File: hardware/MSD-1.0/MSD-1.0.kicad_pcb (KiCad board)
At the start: 2 copper layers, 98.4 x 31.7 mm, 19 parts, among them J1 Conn_01x05, J2 Conn_01x03, Q1 IRF840N, U1 NE555P, U2 PC817, U3 PC817

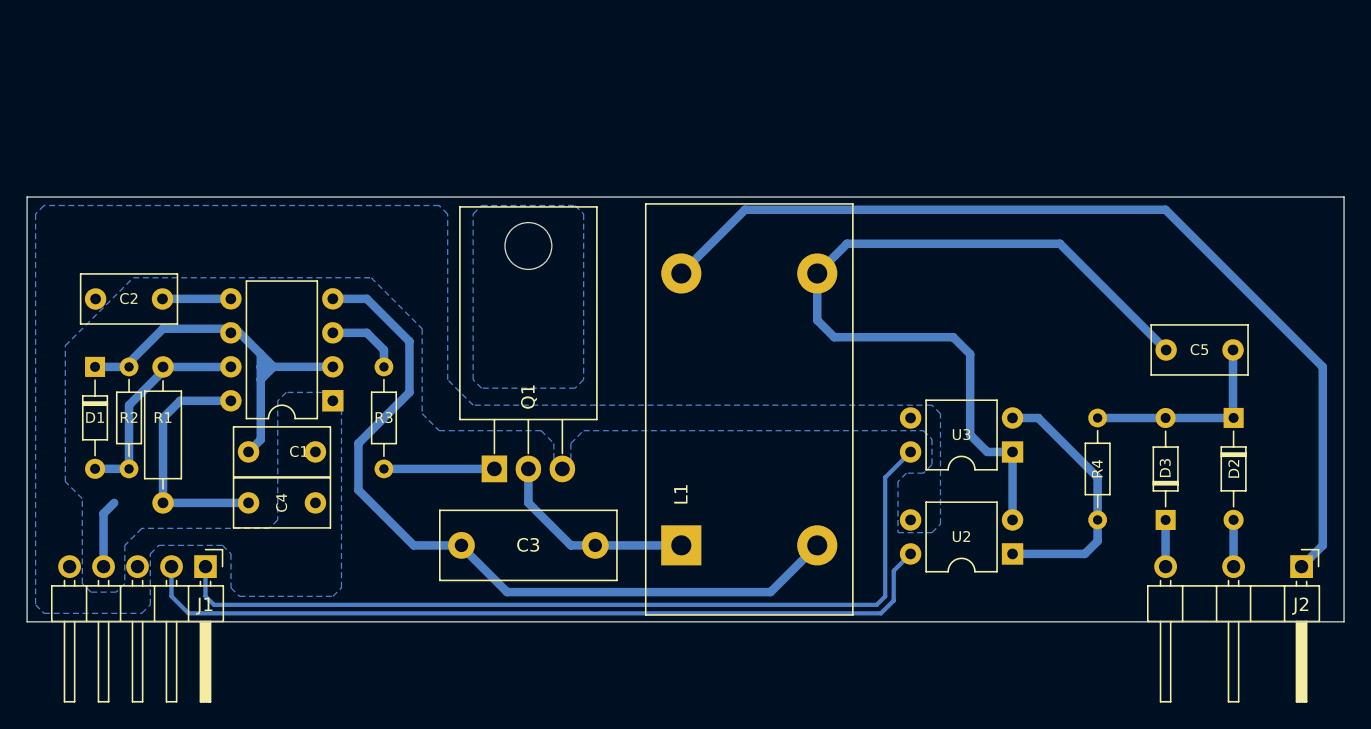
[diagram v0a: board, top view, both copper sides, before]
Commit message: deleted:    hardware/MSD-1.0/#auto_saved_files# 	new file:   hardware/MSD-1.0/MSD-1.0 BoM.csv 	new file:   hardware/MSD-1.0/MSD-1.0-B_Cu.gbr 	new file:   hardware/MSD-1.0/MSD-1.0-B_Mask.gbr 	new file:   hardware/MSD-1.0/MSD-1.0-B_Paste.gbr 	new file:   hardware/MSD-1.0/MSD-1.0-B_Silkscreen.gbr 	new file:   hardware/MSD-1.0/MSD-1.0-Edge_Cuts.gbr 	new file:   hardware/MSD-1.0/MSD-1.0-F_Cu.gbr 	new file:   hardware/MSD-1.0/MSD-1.0-F_Mask.gbr 	new file:   hardware/MSD-1.0/MSD-1.0-F_Paste.gbr 	new file:   hardware/MSD-1.0/MSD-1.0-F_Silkscreen.gbr 	new file:   hardware/MSD-1.0/MSD-1.0-NPTH.drl 	new file:   hardware/MSD-1.0/MSD-1.0-PTH.drl 	deleted:    hardware/MSD-1.0/MSD-1.0-backups/MSD-1.0-2025-02-24_160102.zip 	deleted:    hardware/MSD-1.0/MSD-1.0-backups/MSD-1.0-2025-02-24_160721.zip 	deleted:    hardware/MSD-1.0/MSD-1.0-backups/MSD-1.0-2025-02-24_161316.zip 	deleted:    hardware/MSD-1.0/MSD-1.0-backups/MSD-1.0-2025-02-24_162407.zip 	deleted:    hardware/MSD-1.0/MSD-1.0-backups/MSD-1.0-2025-02-24_163137.zip 	deleted:    hardware/MSD-1.0/MSD-1.0-backups/MSD-1.0-2025-02-25_161045.zip 	deleted:    hardware/MSD-1.0/MSD-1.0-backups/MSD-1.0-2025-02-26_093224.zip 	deleted:    hardware/MSD-1.0/MSD-1.0-backups/MSD-1.0-2025-02-26_094218.zip 	new file:   hardware/MSD-1.0/MSD-1.0-backups/MSD-1.0-2025-02-26_163854.zip 	new file:   hardware/MSD-1.0/MSD-1.0-backups/MSD-1.0-2025-02-27_112851.zip 	new file:   hardware/MSD-1.0/MSD-1.0-backups/MSD-1.0-2025-02-27_114053.zip 	new file:   hardware/MSD-1.0/MSD-1.0-backups/MSD-1.0-2025-02-27_185834.zip 	new file:   hardware/MSD-1.0/MSD-1.0-backups/MSD-1.0-2025-02-27_190654.zip 	new file:   hardware/MSD-1.0/MSD-1.0-backups/MSD-1.0-2025-02-27_191228.zip 	new file:   hardware/MSD-1.0/MSD-1.0-backups/MSD-1.0-2025-02-28_140545.zip 	new file:   hardware/MSD-1.0/MSD-1.0-backups/MSD-1.0-2025-02-28_141533.zip 	new file:   hardware/MSD-1.0/MSD-1.0-backups/MSD-1.0-2025-02-28_142536.zip 	new file:   hardware/MSD-1.0/MSD-1.0-backups/MSD-1.0-2025-02-28_14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
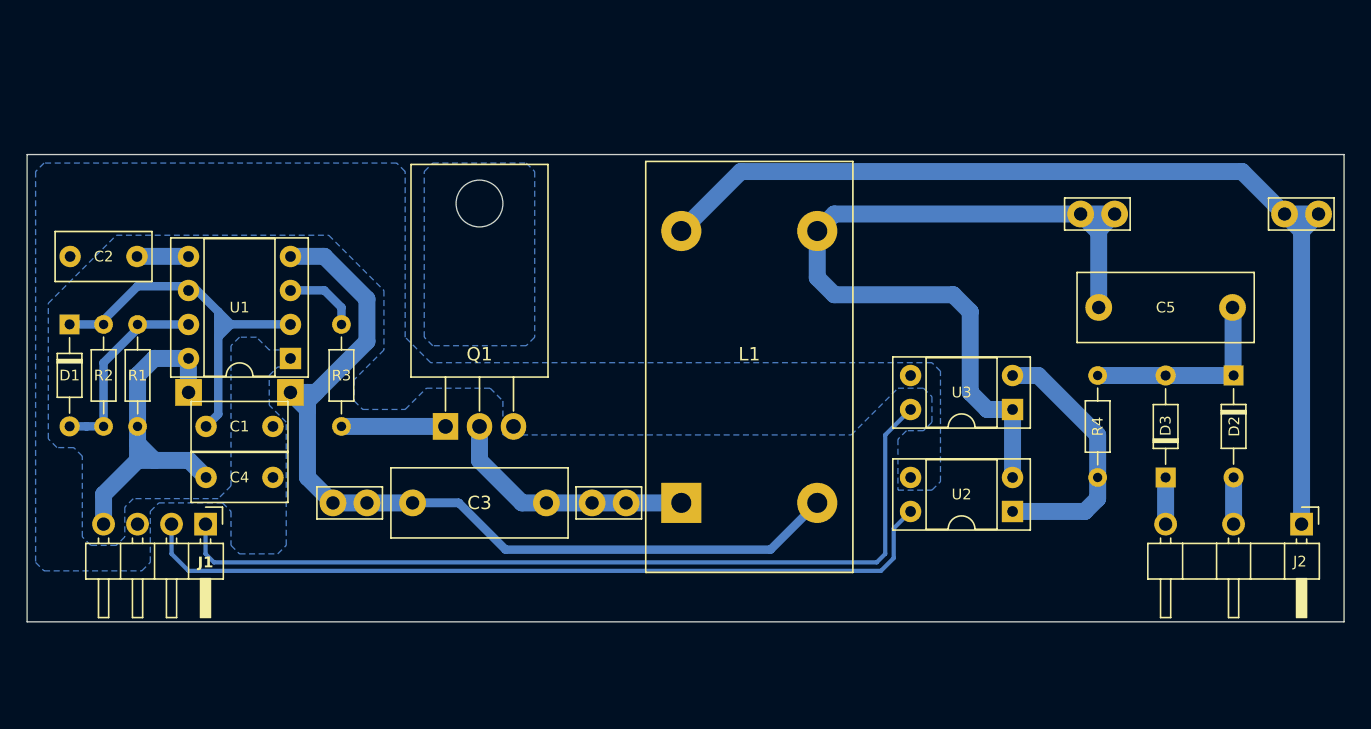
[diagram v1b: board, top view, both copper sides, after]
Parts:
- added TP1: TestPoint, TestPoint:TestPoint_Bridge_Pitch2.54mm_Drill1.0mm, F.Cu at (99.1, 61.0)
- added TP2: TestPoint, TestPoint:TestPoint_Bridge_Pitch2.54mm_Drill1.0mm, F.Cu at (118.4, 61.0)
- added TP3: TestPoint, TestPoint:TestPoint_Bridge_Pitch2.54mm_Drill1.0mm, F.Cu at (154.9, 39.4)
- added TP4: TestPoint, TestPoint:TestPoint_Bridge_Pitch2.54mm_Drill1.0mm, F.Cu at (170.2, 39.4)
- added TP5: TestPoint, TestPoint:TestPoint_THTPad_2.0x2.0mm_Drill1.0mm_NoSilkscreen, F.Cu at (88.3, 52.7)
- added TP6: TestPoint, TestPoint:TestPoint_THTPad_2.0x2.0mm_Drill1.0mm_NoSilkscreen, F.Cu at (95.9, 52.7)
- C2: value 470pF -> 10nF
- C3: value 0.022uF 275V MKP -> 0.022uF 400V MKP
- C5: value 10nF -> ~; footprint Capacitor_THT:C_Rect_L7.0mm_W3.5mm_P5.00mm -> Capacitor_THT:C_Rect_L13.0mm_W5.0mm_P10.00mm_FKS3_FKP3_MKS4
- D2, D3: value D -> HER208
- J1: footprint Connector_PinHeader_2.54mm:PinHeader_1x05_P2.54mm_Horizontal -> Connector_PinHeader_2.54mm:PinHeader_1x04_P2.54mm_Horizontal_Custom
- J2: footprint Connector_PinHeader_2.54mm:PinHeader_1x03_P5.08mm_Horizontal -> Connector_PinHeader_2.54mm:PinHeader_1x03_P5.08mm_Horizontal_Custom
- L1: value L_Coupled -> Isolation Transformer (Custom)
- Q1: value IRF840N -> IRF840
- R1: footprint Resistor_THT:R_Axial_DIN0207_L6.3mm_D2.5mm_P10.16mm_Horizontal -> Resistor_THT:R_Axial_DIN0204_L3.6mm_D1.6mm_P7.62mm_Horizontal
- R4: value R -> 330Ω
- U1: footprint Package_DIP:DIP-8_W7.62mm -> Package_DIP:DIP-8_W7.62mm_Socket
- U2, U3: footprint Package_DIP:DIP-4_W7.62mm -> Package_DIP:DIP-4_W7.62mm_Socket
- moved U1 9.86 mm to (92.1, 46.4)
- moved R1 9.71 mm to (84.5, 51.4)
- moved J2 5.99 mm to (171.4, 62.5)
- moved C5 5.96 mm to (156.3, 46.4)
- moved C3 4.84 mm to (105.0, 61.0)
- moved Q1 4.84 mm to (107.5, 55.2)
- moved R3 4.49 mm to (99.7, 51.4)
- moved D1 3.70 mm to (79.4, 47.6)
- moved C1 3.70 mm to (89.6, 55.2)
- moved C4 3.70 mm to (89.6, 59.1)
- moved C2 3.70 mm to (84.4, 42.5)
- moved R2 3.70 mm to (81.9, 51.4)
- moved L1 3.18 mm to (125.1, 61.0)
- moved U2 3.18 mm to (149.8, 61.6)
- moved U3 3.18 mm to (149.8, 54.0)
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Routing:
- net +12V: track 82.1 -> 100.7 mm
- net Net-(J2-Pin_1): track 70.4 -> 76.3 mm
- net Net-(Q1-D): track 15.3 -> 19.4 mm
- net Net-(C5-Pad1): track 61.1 -> 63.0 mm
- net Net-(D1-A): track 16.3 -> 14.7 mm
- net Net-(U1-CV): track 5.11 -> 3.84 mm
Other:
- board size 98.4 x 31.7 mm -> 98.4 x 34.9 mm

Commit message: modified:   .DS_Store 	deleted:    hardware/MSD-1.0/MSD-1.0-backups/MSD-1.0-2025-02-25_161819.zip 	deleted:    hardware/MSD-1.0/MSD-1.0-backups/MSD-1.0-2025-02-25_162448.zip 	deleted:    hardware/MSD-1.0/MSD-1.0-backups/MSD-1.0-2025-02-25_163016.zip 	deleted:    hardware/MSD-1.0/MSD-1.0-backups/MSD-1.0-2025-02-25_163954.zip 	deleted:    hardware/MSD-1.0/MSD-1.0-backups/MSD-1.0-2025-02-26_112856.zip 	deleted:    hardware/MSD-1.0/MSD-1.0-backups/MSD-1.0-2025-02-26_113923.zip 	deleted:    hardware/MSD-1.0/MSD-1.0-backups/MSD-1.0-2025-02-26_115654.zip 	deleted:    hardware/MSD-1.0/MSD-1.0-backups/MSD-1.0-2025-02-26_120757.zip 	deleted:    hardware/MSD-1.0/MSD-1.0-backups/MSD-1.0-2025-02-26_163854.zip 	deleted:    hardware/MSD-1.0/MSD-1.0-backups/MSD-1.0-2025-02-27_112851.zip 	deleted:    hardware/MSD-1.0/MSD-1.0-backups/MSD-1.0-2025-02-27_114053.zip 	deleted:    hardware/MSD-1.0/MSD-1.0-backups/MSD-1.0-2025-02-27_185834.zip 	deleted:    hardware/MSD-1.0/MSD-1.0-backups/MSD-1.0-2025-02-27_190654.zip 	deleted:    hardware/MSD-1.0/MSD-1.0-backups/MSD-1.0-2025-02-27_191228.zip 	deleted:    hardware/MSD-1.0/MSD-1.0-backups/MSD-1.0-2025-02-28_140545.zip 	deleted:    hardware/MSD-1.0/MSD-1.0-backups/MSD-1.0-2025-02-28_141533.zip 	deleted:    hardware/MSD-1.0/MSD-1.0-backups/MSD-1.0-2025-02-28_142536.zip 	deleted:    hardware/MSD-1.0/MSD-1.0-backups/MSD-1.0-2025-02-28_143342.zip 	deleted:    hardware/MSD-1.0/MSD-1.0-backups/MSD-1.0-2025-02-28_162722.zip 	deleted:    hardware/MSD-1.0/MSD-1.0-backups/MSD-1.0-2025-03-05_134102.zip 	deleted:    hardware/MSD-1.0/MSD-1.0-backups/MSD-1.0-2025-03-05_134620.zip 	new file:   hardware/MSD-1.0/MSD-1.0-backups/MSD-1.0-2025-03-24_113503.zip 	new file:   hardware/MSD-1.0/MSD-1.0-backups/MSD-1.0-2025-03-24_114029.zip 	new file:   hardware/MSD-1.0/MSD-1.0-backups/MSD-1.0-2025-03-24_132745.zip 	new file:   hardware/MSD-1.0/MSD-1.0-backups/MSD-1.0-2025-03-24_134332.zip 	new file:   hardware/MSD-1.0/MSD-1.0-backups/MSD-1.0-2025-03-25_144744.zip 	n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
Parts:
- added C6: 470µF 35V, Capacitor_THT:CP_Radial_D12.5mm_P5.00mm, F.Cu at (97.2, 60.0)
- D1: footprint Diode_THT:D_DO-34_SOD68_P7.62mm_Horizontal -> Diode_THT:D_DO-35_SOD27_P7.62mm_Horizontal
- J1: footprint Connector_PinHeader_2.54mm:PinHeader_1x04_P2.54mm_Horizontal_Custom -> Connector_PinHeader_2.54mm:PinHeader_1x04_P2.54mm_Horizontal_2
- J2: footprint Connector_PinHeader_2.54mm:PinHeader_1x03_P5.08mm_Horizontal_Custom -> Connector_PinHeader_2.54mm:PinHeader_1x03_P5.08mm_Horizontal_2
- L1: value Isolation Transformer (Custom) -> L_Ferrite_Coupled; footprint Inductor_THT:L_CommonMode_Toroid_Vertical_L30.5mm_W15.2mm_Px10.16mm_Py20.32mm_Bourns_8100 -> Inductor_THT:L_CommonMode_Toroid_Horizontal_OD23mm_ID14mm_H8mm
- moved L1 21.0 mm to (126.7, 40.0)
- moved TP4 16.8 mm to (154.6, 33.0)
- moved U2 16.2 mm to (134.3, 66.0)
- moved U3 16.2 mm to (134.3, 58.4)
- moved TP3 12.3 mm to (144.5, 33.0)
- moved C5 12.1 mm to (145.8, 40.3)
- moved R4 10.9 mm to (145.7, 52.1)
- moved D2 10.9 mm to (155.9, 48.3)
- moved D3 10.9 mm to (150.8, 55.9)
- moved J2 10.8 mm to (161.0, 60.0)
- moved C3 8.47 mm to (103.1, 52.7)
- moved TP1 8.47 mm to (97.2, 52.7)
- moved TP2 8.47 mm to (116.5, 52.7)
- moved Q1 6.68 mm to (105.4, 48.9)
- moved C2 6.35 mm to (84.4, 36.2)
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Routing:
- net +12V: track 100.7 -> 121.3 mm
- net Net-(J2-Pin_1): track 76.3 -> 58.0 mm
- net Net-(J1-Pin_2): track 61.1 -> 49.9 mm
- net Net-(J1-Pin_1): track 65.1 -> 54.4 mm
- net Net-(R4-Pad1): track 19.7 -> 27.9 mm
- net Net-(D2-K): track 15.3 -> 18.1 mm
- net Net-(C5-Pad1): track 63.0 -> 65.7 mm
- net Net-(D3-K): track 3.49 -> 6.03 mm
- net Net-(D2-A): track 3.49 -> 6.03 mm
- net Net-(Q1-G): track 7.78 -> 5.72 mm
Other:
- board size 98.4 x 34.9 mm -> 98.4 x 44.4 mm

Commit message: deleted:    hardware/Gain/Gain-backups/Gain-2025-04-14_115147.zip 	new file:   hardware/Gain/Gain-backups/Gain-2025-04-15_120154.zip 	deleted:    hardware/MSD-1.0/MSD-1.0-backups/MSD-1.0-2025-03-24_134332.zip 	deleted:    hardware/MSD-1.0/MSD-1.0-backups/MSD-1.0-2025-03-25_144744.zip 	deleted:    hardware/MSD-1.0/MSD-1.0-backups/MSD-1.0-2025-03-25_145433.zip 	deleted:    hardware/MSD-1.0/MSD-1.0-backups/MSD-1.0-2025-03-25_150210.zip 	deleted:    hardware/MSD-1.0/MSD-1.0-backups/MSD-1.0-2025-03-25_150818.zip 	new file:   hardware/MSD-1.0/MSD-1.0-backups/MSD-1.0-2025-04-16_142822.zip 	new file:   hardware/MSD-1.0/MSD-1.0-backups/MSD-1.0-2025-04-16_143722.zip 	new file:   hardware/MSD-1.0/MSD-1.0-backups/MSD-1.0-2025-04-16_145208.zip 	new file:   hardware/MSD-1.0/MSD-1.0-backups/MSD-1.0-2025-04-16_150237.zip 	new file:   hardware/MSD-1.0/MSD-1.0-backups/MSD-1.0-2025-04-16_150829.zip 	modified:   hardware/MSD-1.0/MSD-1.0.kicad_pcb 	modified:   hardware/MSD-1.0/MSD-1.0.kicad_sch 	modified:   hardware/MSD-1.0/MSD-1.0.step 	new file:   hardware/MSD-2.0/MSD-2.0-backups/MSD-2.0-2025-04-16_090248.zip 	deleted:    hardware/PS-1.0/PS-1.0-backups/PS-1.0-2025-03-18_205016.zip 	deleted:    hardware/PS-1.0/PS-1.0-backups/PS-1.0-2025-03-18_205728.zip 	deleted:    hardware/PS-1.0/PS-1.0-backups/PS-1.0-2025-03-18_211157.zip 	deleted:    hardware/PS-1.0/PS-1.0-backups/PS-1.0-2025-03-18_213933.zip 	deleted:    hardware/PS-1.0/PS-1.0-backups/PS-1.0-2025-03-19_094557.zip 	deleted:    hardware/PS-1.0/PS-1.0-backups/PS-1.0-2025-03-19_101204.zip 	deleted:    hardware/PS-1.0/PS-1.0-backups/PS-1.0-2025-03-19_102323.zip 	new file:   hardware/PS-1.0/PS-1.0-backups/PS-1.0-2025-04-16_154157.zip 	new file:   hardware/PS-1.0/PS-1.0-backups/PS-1.0-2025-04-16_154838.zip 	new file:   hardware/PS-1.0/PS-1.0-backups/PS-1.0-2025-04-16_155906.zip 	new file:   hardware/PS-1.0/PS-1.0-backups/PS-1.0-2025-04-16_160456.zip 	new file:   hardware/PS-1.0/PS-1.0-backups/PS-1.0-2025-04-16_161300.zip 	new file:   har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
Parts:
- added TP7: TestPoint, TestPoint:TestPoint_Bridge_Pitch2.54mm_Drill1.0mm, F.Cu at (79.4, 27.6)
- C5: value ~ -> 100nF 400V
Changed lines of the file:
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@@
 			)
 		)
-		(property "Value" "~"
+		(property "Value" "100nF 400V"
 			(at 5 3.75 0)
 			(layer "F.Fab")
@@
 		)
 		(model "${KICAD8_3DMODEL_DIR}/Capacitor_THT.3dshapes/CP_Radial_D12.5mm_P5.00mm.wrl"
+			(hide yes)
 			(offset
 				(xyz 0 0 0)
@@
 			)
 		)
+		(model "/Users/margabudi/Documents/KiCad/libraries/ELCO/User Library-Cap-EL(12_5x20-5)T.step"
+			(hide yes)
+			(offset
+				(xyz 2.5 0 0)
+			)
+			(scale
+				(xyz 1 1 1)
+			)
+			(rotate
+				(xyz 0 0 0)
+			)
+		)
 	)
 	(footprint "Resistor_THT:R_Axial_DIN0204_L3.6mm_D1.6mm_P7.62mm_Horizontal"
@@
 			)
 			(scale
+				(xyz 1 1 1)
+			)
+			(rotate
+				(xyz 0 0 0)
+			)
+		)
+	)
+	(footprint "TestPoint:TestPoint_Bridge_Pitch2.54mm_Drill1.0mm"
+		(layer "F.Cu")
+		(at 79.375 27.6225)
+		(descr "wire loop as test point, pitch 2.54mm, hole diameter 1.0mm, wire diameter 0.8mm")
+		(tags "test point wire loop")
+		(property "Reference" "TP7"
+			(at 1.1 2.1 0)
+			(layer "F.SilkS")
+			(hide yes)
+			(effects
+				(font
+					(size 1 1)
+					(thickness 0.15)
+				)
+			)
+		)
+		(property "Value" "TestPoint"
+			(at 1 -1.7 0)
+			(layer "F.Fab")
+			(effects
+				(font
+					(size 1 1)
+					(thickness 0.15)
+				)
+			)
+		)
+		(property "Footprint" "TestPoint:TestPoint_Bridge_Pitch2.54mm_Drill1.0mm"
+			(at 0 0 0)
+			(unlocked yes)
+			(layer "F.Fab")
+			(hide yes)
+			(effects
+				(font
+					(size 1.27 1.27)
+					(thickness 0.15)
+				)
+			)
+		)
+		(property "Datasheet" ""
+			(at 0 0 0)
+			(unlocked yes)
+			(layer "F.Fab")
+			(hide yes)
+			(effects
+				(font
+					(size 1.27 1.27)
+					(thickness 0.15)
+				)
+			)
+		)
+		(property "Description" "test point"
+			(at 0 0 0)
+			(unlocked yes)
+			(layer "F.Fab")
+			(hide yes)
+			(effects
+				(font
+					(size 1.27 1.27)
+					(thickness 0.15)
+				)
+			)
+		)
+		(property ki_fp_filters "Pin* Test*")
+		(sheetname "Root")
+		(sheetfile "MSD-1.0.kicad_sch")
+		(attr through_hole)
+		(fp_line
+			(start -1.2 -1.2)
+			(end -1.2 1.2)
+			(stroke
+				(width 0.12)
+				(type solid)
+			)
+			(layer "F.SilkS")
+		)
+		(fp_line
+			(start -1.2 1.2)
+			(end 3.7 1.2)
+			(stroke
+				(width 0.12)
+				(type solid)
+			)
+			(layer "F.SilkS")
+		)
+		(fp_line
+			(start 3.7 -1.2)
+			(end -1.2 -1.2)
+			(stroke
+				(width 0.12)
+				(type solid)
+			)
+			(layer "F.SilkS")
+		)
+		(fp_line
+			(start 3.7 1.2)
+			(end 3.7 -1.2)
+			(stroke
+				(width 0.12)
+				(type solid)
+			)
+			(layer "F.SilkS")
+		)
+		(fp_line
+			(start -1.5 -1.5)
+			(end -1.5 1.5)
+			(stroke
+				(width 0.05)
+				(type solid)
+			)
+			(layer "F.CrtYd")
+		)
+		(fp_line
+			(start -1.5 -1.5)
+			(end 4.04 -1.5)
+			(stroke
+				(width 0.05)
+				(type solid)
+			)
+			(layer "F.CrtYd")
+		)
+		(fp_line
+			(start 4.04 1.5)
+			(end -1.5 1.5)
+			(stroke
+				(width 0.05)
+				(type solid)
+			)
+			(layer "F.CrtYd")
+		)
+		(fp_line
+			(start 4.04 1.5)
+			(end 4.04 -1.5)
+			(stroke
+				(width 0.05)
+				(type solid)
+			)
+			(layer "F.CrtYd")
+		)
+		(fp_line
+			(start 2.54 0)
+			(end 0 0)
+			(stroke
+				(width 0.12)
+				(type solid)
+			)
+			(layer "F.Fab")
+		)
+		(fp_text user "${REFERENCE}"
+			(at 1.1 2.1 0)
+			(layer "F.Fab")
+			(effects
+				(font
+					(size 1 1)
+					(thickness 0.15)
+				)
+			)
+		)
+		(pad "1" thru_hole circle
+			(at 0 0)
+			(size 2 2)
+			(drill 1)
+			(layers "*.Cu" "*.Mask")
+			(remove_unused_layers no)
+			(net 7 "GND")
+			(pinfunction "1")
+			(pintype "passive")
+		)
+		(pad "1" thru_hole circle
+			(at 2.54 0)
+			(size 2 2)
+			(drill 1)
+			(layers "*.Cu" "*.Mask")
+			(remove_unused_layers no)
+			(net 7 "GND")
+			(pinfunction "1")
+			(pintype "passive")
+		)
+		(model "${KICAD8_3DMODEL_DIR}/TestPoint.3dshapes/TestPoint_Bridge_Pitch2.54mm_Drill1.0mm.wrl"
+			(offset
+				(xyz 0 0 0)
+			)
+			(scale

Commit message: new file:   .~BoM.xlsx 	new file:   BoM.xlsx 	new file:   hardware/BoM.xlsx 	deleted:    hardware/MSD-1.0/MSD-1.0-backups/MSD-1.0-2025-03-26_092035.zip 	deleted:    hardware/MSD-1.0/MSD-1.0-backups/MSD-1.0-2025-03-26_092834.zip 	deleted:    hardware/MSD-1.0/MSD-1.0-backups/MSD-1.0-2025-03-27_092014.zip 	new file:   hardware/MSD-1.0/MSD-1.0-backups/MSD-1.0-2025-04-28_130614.zip 	new file:   hardware/MSD-1.0/MSD-1.0-backups/MSD-1.0-2025-04-28_131128.zip 	new file:   hardware/MSD-1.0/MSD-1.0-backups/MSD-1.0-2025-04-28_132753.zip 	new file:   hardware/MSD-1.0/MSD-1.0.csv 	modified:   hardware/MSD-1.0/MSD-1.0.kicad_pcb 	modified:   hardware/MSD-1.0/MSD-1.0.kicad_sch 	deleted:    hardware/PS-1.0/PS-1.0-backups/PS-1.0-2025-03-24_111800.zip 	deleted:    hardware/PS-1.0/PS-1.0-backups/PS-1.0-2025-03-24_112738.zip 	deleted:    hardware/PS-1.0/PS-1.0-backups/PS-1.0-2025-03-25_152833.zip 	deleted:    hardware/PS-1.0/PS-1.0-backups/PS-1.0-2025-03-25_154601.zip 	deleted:    hardware/PS-1.0/PS-1.0-backups/PS-1.0-2025-03-25_155821.zip 	deleted:    hardware/PS-1.0/PS-1.0-backups/PS-1.0-2025-04-11_101418.zip 	deleted:    hardware/PS-1.0/PS-1.0-backups/PS-1.0-2025-04-11_110528.zip 	deleted:    hardware/PS-1.0/PS-1.0-backups/PS-1.0-2025-04-11_111527.zip 	deleted:    hardware/PS-1.0/PS-1.0-backups/PS-1.0-2025-04-11_114252.zip 	deleted:    hardware/PS-1.0/PS-1.0-backups/PS-1.0-2025-04-17_105409.zip 	new file:   hardware/PS-1.0/PS-1.0-backups/PS-1.0-2025-04-19_071925.zip 	new file:   hardware/PS-1.0/PS-1.0-backups/PS-1.0-2025-04-27_222808.zip 	new file:   hardware/PS-1.0/PS-1.0-backups/PS-1.0-2025-04-27_223939.zip 	new file:   hardware/PS-1.0/PS-1.0-backups/PS-1.0-2025-04-27_224445.zip 	new file:   hardware/PS-1.0/PS-1.0-backups/PS-1.0-2025-04-27_225206.zip 	new file:   hardware/PS-1.0/PS-1.0-backups/PS-1.0-2025-04-27_230217.zip 	new file:   hardware/PS-1.0/PS-1.0-backups/PS-1.0-2025-04-28_083014.zip 	new file:   hardware/PS-1.0/PS-1.0-backups/PS-1.0-2025-04-28_112951.zip 	new file:   har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
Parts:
- C1: value 2.2nF -> 2.2nF 100
- C2: value 10nF -> 10nF 63
- C3: value 0.022uF 400V MKP -> 0.022uF 400
- C4: value 100nF -> 100nF 100
- C5: value 100nF 400V -> 100nF 400
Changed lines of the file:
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@@
 			)
 		)
-		(property "Value" "10nF"
+		(property "Value" "10nF 63"
 			(at 2.5 3 0)
 			(layer "F.Fab")
@@
 			)
 		)
-		(property "Value" "0.022uF 400V MKP"
+		(property "Value" "0.022uF 400"
 			(at 5 3.75 0)
 			(layer "F.Fab")
@@
 			)
 		)
-		(property "Value" "100nF 400V"
+		(property "Value" "100nF 400"
 			(at 5 3.75 0)
 			(layer "F.Fab")
@@
 			)
 		)
-		(property "Value" "100nF"
+		(property "Value" "100nF 100"
 			(at 2.5 3 0)
 			(layer "F.Fab")
@@
 			)
 		)
-		(property "Value" "2.2nF"
+		(property "Value" "2.2nF 100"
 			(at 2.5 3 0)
 			(layer "F.Fab")
